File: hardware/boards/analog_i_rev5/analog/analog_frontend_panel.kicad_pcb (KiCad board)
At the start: 4 copper layers, 308 parts, among them IC1 INA826AIDR, IC1001 BD42540FJ-CE2, IC1002 BD42540FJ-CE2, IC1003 BD42540FJ-CE2, IC12 INA826AIDR, IC13 TLV333IDBVR, IC14 TLV333IDBVR, IC15 INA826AIDR, IC16 TLV333IDBVR, IC17 TLV333IDBVR, IC18 INA826AIDR, IC19 TLV333IDBVR, IC2 INA826AIDR, IC20 TLV333IDBVR, IC21 INA826AIDR, IC22 TLV333IDBVR, IC22001 INA826AIDR, IC23 TLV333IDBVR, IC23001 INA826AIDR, IC27001 INA826AIDR, IC31001 INA826AIDR, IC32001 BD42540FJ-CE2, IC32002 INA826AIDR, IC33001 BD42540FJ-CE2, IC34001 BD42540FJ-CE2, IC34002 INA826AIDR, IC35001 BD42540FJ-CE2, IC37001 INA826AIDR, IC45001 INA826AIDR, IC5 INA826AIDR, IC6 INA826AIDR, IC7 INA826AIDR, IC8 INA826AIDR, J1001 Screw_Terminal_01x12, J1003 Screw_Terminal_01x10, J1004 Screw_Terminal_01x12, J1005 Screw_Terminal_01x12, J1006 Screw_Terminal_01x10, J1007 Screw_Terminal_01x12, J12 AM-K-PCB, J13 AM-K-PCB, U1 NTJD4001NT1G, U14001 OPA333xxDBV, U15001 OPA333xxDBV, U16001 OPA333xxDBV, U17001 OPA333xxDBV, U18001 OPA333xxDBV, U19001 74LVC1G17, U2 NTJD4001NT1G, U20001 OPA333xxDBV, U21001 OPA333xxDBV, U24001 OPA333xxDBV, U25001 OPA333xxDBV, U26001 74LVC1G17, U27001 74LVC1G17, U3 NTJD4001NT1G, U30001 OPA333xxDBV, U32001 OPA333xxDBV, U33001 OPA333xxDBV, U33002 74LVC1G17, U38001 74LVC1G17, U39001 74LVC1G17, U39002 74LVC1G17, U4 NTJD4001NT1G, U40001 74LVC1G17, U42001 74LVC1G17, U44001 OPA333xxDBV, U5001 OPA333xxDBV, U8001 OPA333xxDBV, U9001 OPA333xxDBV

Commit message: finish layout
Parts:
- moved H1004 0.49 mm to (160.5, 166.3)
- moved H1001 0.16 mm to (130.7, 115.3)
- moved H1003 0.13 mm to (160.5, 115.3)
- moved H1002 0.09 mm to (130.7, 166.3)
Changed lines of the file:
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@@
 	(footprint "MountingHole:MountingHole_5mm"
 		(layer "F.Cu")
-		(at 130.703 166.413)
+		(at 130.6522 166.3368)
 		(descr "Mounting Hole 5mm, no annular")
 		(tags "mounting hole 5mm no annular")
@@
 	(footprint "MountingHole:MountingHole_5mm"
 		(layer "F.Cu")
-		(at 160.5226 166.8194)
+		(at 160.4718 166.3368)
 		(descr "Mounting Hole 5mm, no annular")
 		(tags "mounting hole 5mm no annular")
@@
 	(footprint "MountingHole:MountingHole_5mm"
 		(layer "F.Cu")
-		(at 130.496 115.2814)
+		(at 130.6522 115.2828)
 		(descr "Mounting Hole 5mm, no annular")
 		(tags "mounting hole 5mm no annular")
@@
 	(footprint "MountingHole:MountingHole_5mm"
 		(layer "F.Cu")
-		(at 160.4718 115.1558)
+		(at 160.4718 115.2828)
 		(descr "Mounting Hole 5mm, no annular")
 		(tags "mounting hole 5mm no annular")
@@
 		(layer "F.SilkS")
 	)
+	(gr_rect
+		(start 89.6058 115.2828)
+		(end 160.4718 166.3368)
+		(stroke
+			(width 0.15)
+			(type default)
+		)
+		(fill none)
+		(layer "Dwgs.User")
+	)
+	(gr_rect
+		(start 130.6522 115.2828)
+		(end 160.4718 166.3368)
+		(stroke
+			(width 0.15)
+			(type default)
+		)
+		(fill none)
+		(layer "Dwgs.User")
+	)
 	(gr_text "GND"

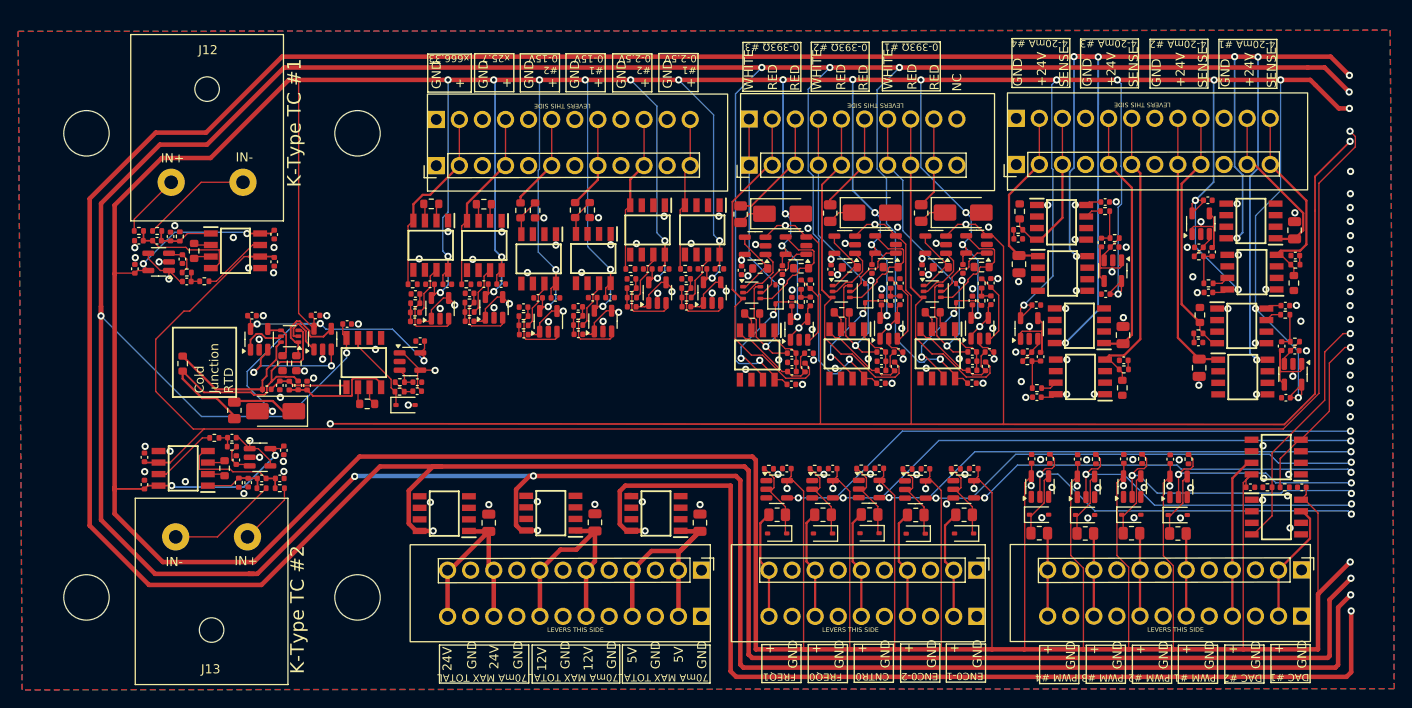
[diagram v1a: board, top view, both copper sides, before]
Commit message: fix drc lints on frontend
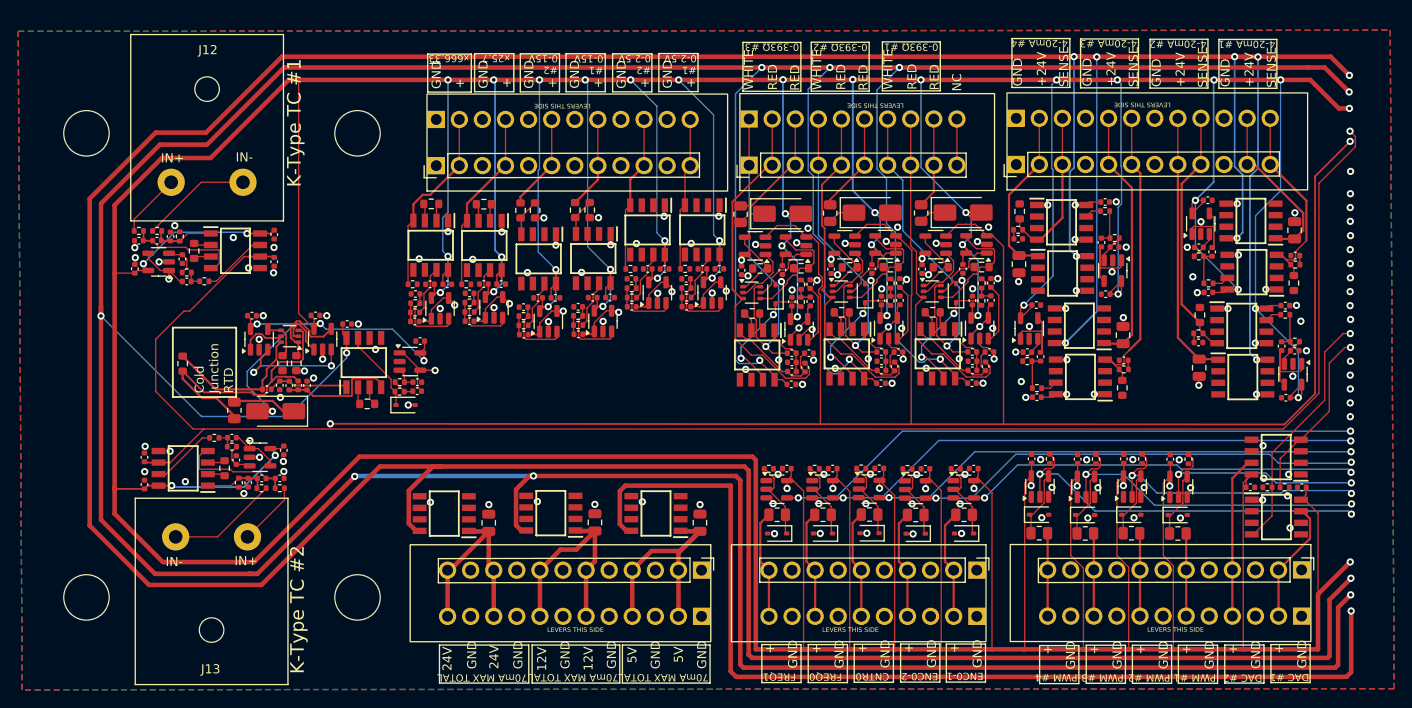
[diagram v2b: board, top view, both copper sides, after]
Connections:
- net /AIN13_DAC1 renamed /AIN13_DAC0
- net /AIN14_DAC2 renamed /AIN14_DAC1
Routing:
- net unconnected-(J1006-Pin_10-Pad10)_1: track 0.00 -> 5.08 mm
- net GND: track 6.85 -> 8.86 mm, vias 134 -> 148
- net +24V: track 483.7 -> 482.1 mm, vias 11 -> 10
- net +5V: track 115.0 -> 113.5 mm, vias 2 -> 1
- net +12V: track 526.1 -> 524.9 mm, vias 13 -> 12
- net /4-20mA Frontend2/SIGNAL: track 32.8 -> 33.8 mm
- net /4-20mA Frontend/SIGNAL: track 22.6 -> 23.3 mm
- net +2V5: track 252.5 -> 252.8 mm, vias 7 -> 4

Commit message: add lcsc pn for terminal blocks
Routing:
- net unconnected-(J1006-Pin_10-Pad10)_1: track 0.00 -> 5.08 mm
- net unconnected-(J1006-Pin_10-Pad10): track 5.08 -> 0.00 mm
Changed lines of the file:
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@@
 	(net 245 "unconnected-(IC1003-N.C._3-Pad4)")
 	(net 246 "unconnected-(IC1003-N.C._1-Pad2)")
+	(net 247 "unconnected-(J1006-Pin_10-Pad10)")
 	(footprint "Resistor_SMD:R_0402_1005Metric"
 		(layer "F.Cu")
@@
 			)
 		)
+		(property "LCSC" "C475123"
+			(at 0 0 -90)
+			(unlocked yes)
+			(layer "F.Fab")
+			(hide yes)
+			(effects
+				(font
+					(size 1 1)
+					(thickness 0.15)
+				)
+			)
+		)
 		(property ki_fp_filters "TerminalBlock*:*")
 		(sheetname "Root")
@@
 			)
 		)
+		(property "LCSC" "C475122"
+			(at 0 0 90)
+			(unlocked yes)
+			(layer "F.Fab")
+			(hide yes)
+			(effects
+				(font
+					(size 1 1)
+					(thickness 0.15)
+				)
+			)
+		)
 		(property ki_fp_filters "TerminalBlock*:*")
 		(sheetname "Root")
@@
 			)
 			(remove_unused_layers no)
-			(net 224 "unconnected-(J1006-Pin_10-Pad10)_1")
+			(net 247 "unconnected-(J1006-Pin_10-Pad10)")
 			(pinfunction "Pin_10")
 			(pintype "passive+no_connect")
@@
 			)
 		)
+		(property "LCSC" "C475123"
+			(at 0 0 -90)
+			(unlocked yes)
+			(layer "F.Fab")
+			(hide yes)
+			(effects
+				(font
+					(size 1 1)
+					(thickness 0.15)
+				)
+			)
+		)
 		(property ki_fp_filters "TerminalBlock*:*")
 		(sheetname "Root")
@@
 			)
 		)
+		(property "LCSC" "C475122"
+			(at 0 0 -90)
+			(unlocked yes)
+			(layer "F.Fab")
+			(hide yes)
+			(effects
+				(font
+					(size 1 1)
+					(thickness 0.15)
+				)
+			)
+		)
 		(property ki_fp_filters "TerminalBlock*:*")
 		(sheetname "Root")
@@
 			)
 		)
+		(property "LCSC" "C475123"
+			(at 0 0 90)
+			(unlocked yes)
+			(layer "F.Fab")
+			(hide yes)
+			(effects
+				(font
+					(size 1 1)
+					(thickness 0.15)
+				)
+			)
+		)
 		(property ki_fp_filters "TerminalBlock*:*")
 		(sheetname "Root")
@@
 					(thickness 0.15)
 				)
+			)
+		)
+		(property "LCSC" "C475123"
+			(at 0 0 90)
+			(unlocked yes)
+			(layer "F.Fab")
+			(hide yes)
+			(effects
+				(font
+					(size 1 1)
+					(thickness 0.15)
+				)
